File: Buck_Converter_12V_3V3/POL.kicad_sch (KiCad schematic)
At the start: 1 part

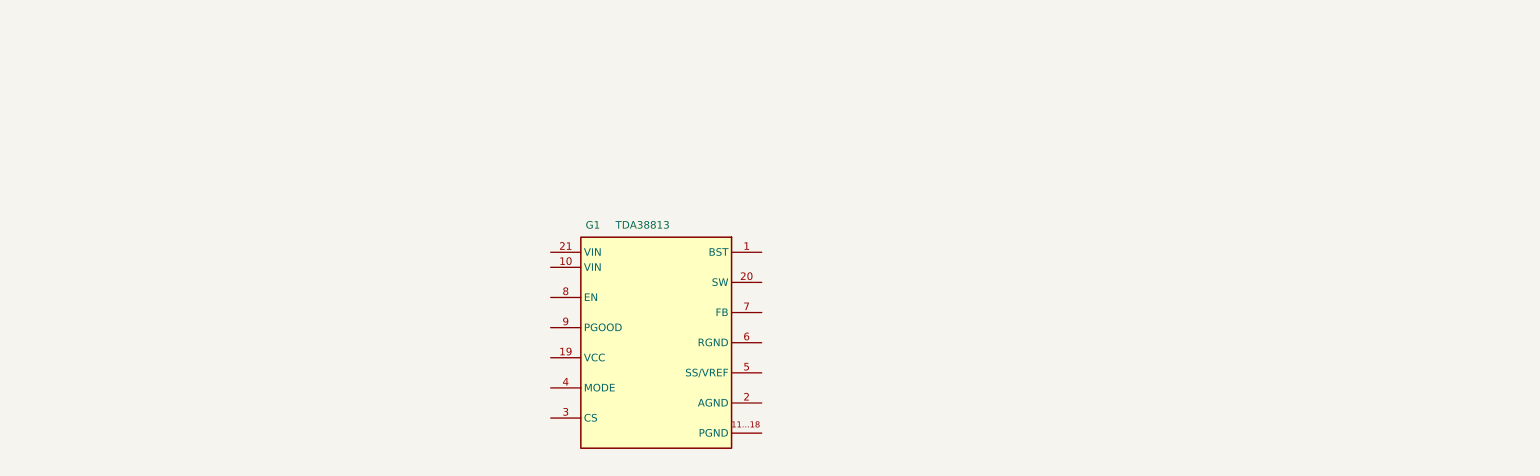
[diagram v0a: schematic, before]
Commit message: :construction: POL IC and input cpacitors added.
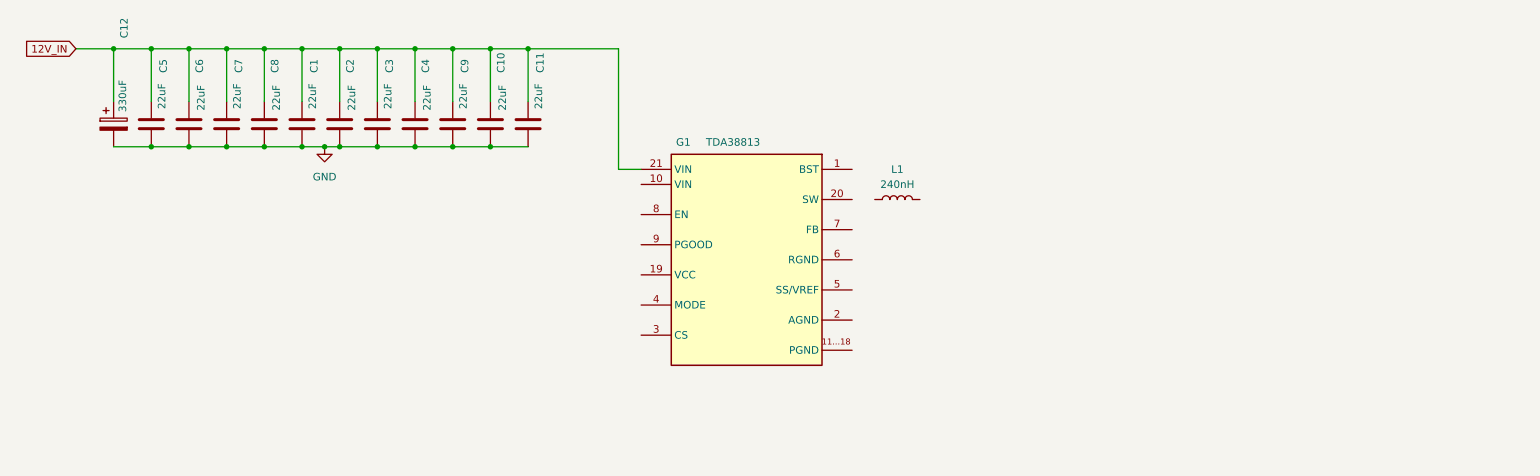
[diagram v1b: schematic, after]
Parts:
- added C1, C10, C11, C2, C3, C4, C5, C6, C7, C8, C9: 22uF, Capacitor_SMD:C_0805_2012Metric_Pad1.18x1.45mm_HandSolder, symbol Device:C
- added C12: 330uF, Capacitor_THT:CP_Radial_D10.0mm_P5.00mm, symbol Device:C_Polarized
- added L1: 240nH, Choke_Coil:Choke_Coil_SMD_3.5_8.4, symbol Device:L
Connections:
- net 12V_IN: now reaches G1.21 (VIN)
- net 12V_IN: now also C1.1, C10.1, C11.1, C12.1, C2.1, C3.1, C4.1, C5.1, C6.1, C7.1, C8.1, C9.1
- new net GND: C1.2, C10.2, C11.2, C12.2, C2.2, C3.2, C4.2, C5.2, C6.2, C7.2, C8.2, C9.2
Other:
- moved on the sheet: G1

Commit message: :construction: Inductor and cap added at power output.
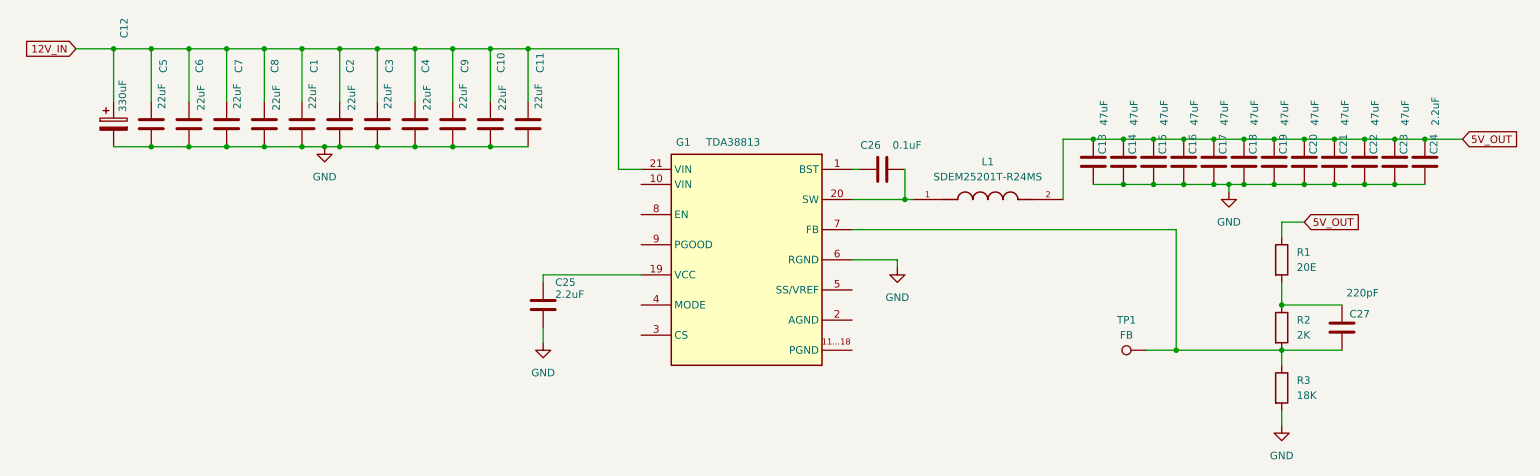
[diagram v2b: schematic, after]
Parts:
- removed L1: 240nH, Choke_Coil:Choke_Coil_SMD_3.5_8.4, symbol Device:L
- added C13, C14, C15, C16, C17, C18, C19, C20, C21, C22, C23: 47uF, Capacitor_SMD:C_0805_2012Metric_Pad1.18x1.45mm_HandSolder, symbol Device:C
- added C24, C25: 2.2uF, Capacitor_SMD:C_0402_1005Metric_Pad0.74x0.62mm_HandSolder, symbol Device:C
- added C26: 0.1uF, Capacitor_SMD:C_0402_1005Metric_Pad0.74x0.62mm_HandSolder, symbol Device:C
- added C27: 220pF, Capacitor_SMD:C_0402_1005Metric_Pad0.74x0.62mm_HandSolder, symbol Device:C
- added L1: SDEM25201T-R24MS, SDEM25201T-R24MS:IND_SDEM25201T-R24MS, symbol Inductor:SDEM25201T-R24MS
- added R1: 20E, Resistor_SMD:R_0402_1005Metric_Pad0.72x0.64mm_HandSolder, symbol Device:R
- added R2: 2K, Resistor_SMD:R_0402_1005Metric_Pad0.72x0.64mm_HandSolder, symbol Device:R
- added R3: 18K, Resistor_SMD:R_0402_1005Metric_Pad0.72x0.64mm_HandSolder, symbol Device:R
- added TP1: FB, symbol Connector:TestPoint
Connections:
- net GND: now also G1.6 (RGND), C13.2, C14.2, C15.2, C16.2, C17.2, C18.2, C19.2, C20.2, C21.2, C22.2, C23.2, C24.2, C25.2, R3.2
- net at G1.1 (BST): now also C26.1
- net at G1.19 (VCC): now also C25.1
- net at G1.20 (SW): now also C26.2, L1.1
- net at G1.7 (FB): now also C27.2, R2.2, R3.1, TP1.1
- new net: C27.1, R1.2, R2.1
- new net 5V_OUT: C13.1, C14.1, C15.1, C16.1, C17.1, C18.1, C19.1, C20.1, C21.1, C22.1, C23.1, C24.1, L1.2, R1.1

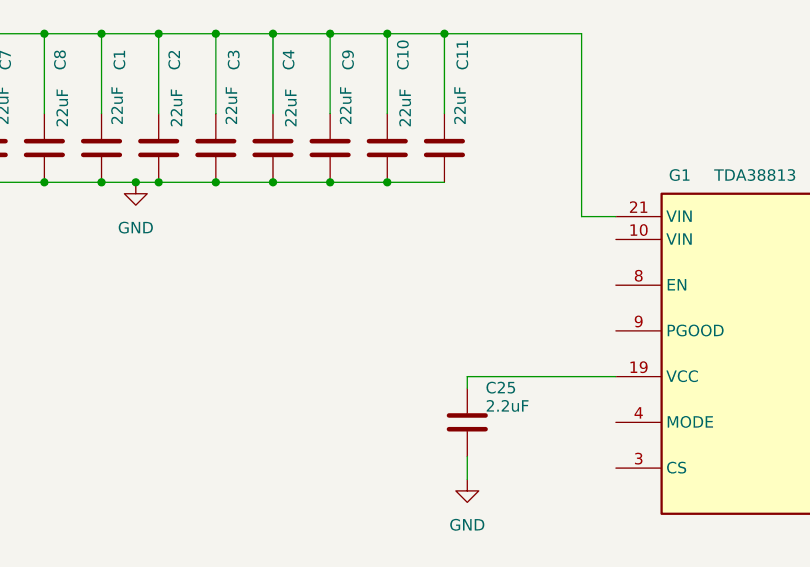
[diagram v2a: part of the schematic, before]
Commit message: Layout Complete
Vis Stiching pending.
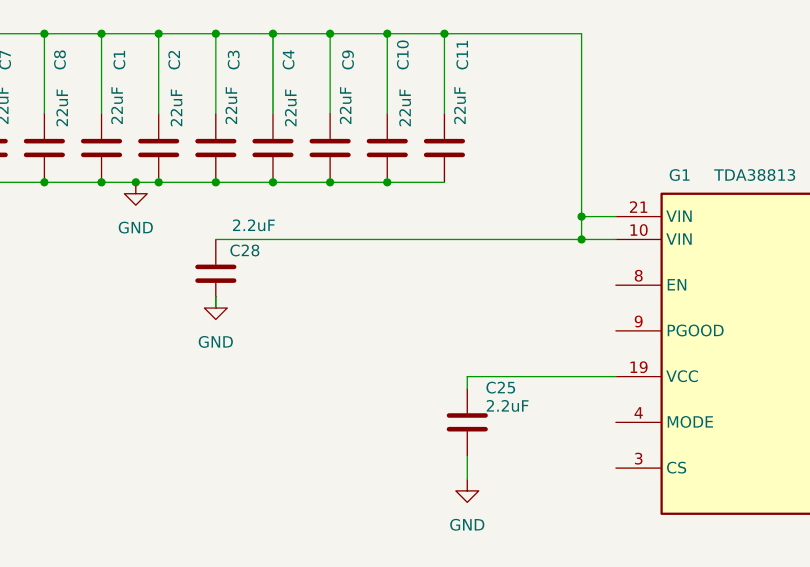
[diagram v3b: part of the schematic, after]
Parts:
- added C28: 2.2uF, Capacitor_SMD:C_0402_1005Metric_Pad0.74x0.62mm_HandSolder, symbol Device:C
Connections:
- net 12V_IN: now also G1.10 (VIN), C28.1
- net GND: now also C28.2
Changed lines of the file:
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@@
 	)
 	(junction
+		(at 128.27 74.93)
+		(diameter 0)
+		(color 0 0 0 0)
+	)
+	(junction
 		(at 113.03 52.07)
 		(diameter 0)
@@
 	)
 	(junction
+		(at 128.27 72.39)
+		(diameter 0)
+		(color 0 0 0 0)
+	)
+	(junction
 		(at 43.18 52.07)
 		(diameter 0)
@@
 	(wire
 		(pts
+			(xy 132.08 74.93) (xy 128.27 74.93)
+		)
+		(stroke
+			(width 0)
+			(type default)
+		)
+	)
+	(wire
+		(pts
 			(xy 55.88 68.58) (xy 62.23 68.58)
 		)
@@
 	(wire
 		(pts
+			(xy 87.63 74.93) (xy 128.27 74.93)
+		)
+		(stroke
+			(width 0)
+			(type default)
+		)
+	)
+	(wire
+		(pts
 			(xy 222.25 102.87) (xy 240.03 102.87)
 		)
@@
 	(wire
 		(pts
+			(xy 87.63 82.55) (xy 87.63 81.28)
+		)
+		(stroke
+			(width 0)
+			(type default)
+		)
+	)
+	(wire
+		(pts
 			(xy 167.64 77.47) (xy 176.53 77.47)
 		)
@@
 	(wire
 		(pts
+			(xy 128.27 72.39) (xy 128.27 74.93)
+		)
+		(stroke
+			(width 0)
+			(type default)
+		)
+	)
+	(wire
+		(pts
 			(xy 43.18 68.58) (xy 49.53 68.58)
 		)
@@
 					(unit 1)
 				)
+			)
+		)
+	)
+	(symbol
+		(lib_id "Device:C")
+		(at 87.63 78.74 0)
+		(unit 1)
+		(exclude_from_sim no)
+		(in_bom yes)
+		(on_board yes)
+		(dnp no)
+		(property "Reference" "C28"
+			(at 89.154 76.2 0)
+			(effects
+				(font
+					(size 1.27 1.27)
+				)
+				(justify left)
+			)
+		)
+		(property "Value" "2.2uF"
+			(at 89.408 73.406 0)
+			(effects
+				(font
+					(size 1.27 1.27)
+				)
+				(justify left)
+			)
+		)
+		(property "Footprint" "Capacitor_SMD:C_0402_1005Metric_Pad0.74x0.62mm_HandSolder"
+			(at 88.5952 82.55 0)
+			(effects
+				(font
+					(size 1.27 1.27)
+				)
+				(hide yes)
+			)
+		)
+		(property "Datasheet" "https://www.digikey.in/en/products/detail/tdk-corporation/C2012X5R0J476M125AC/2443465?s=N4IgTCBcDaIMJgAwEYwA0CsAlRApALAOwBsAsiALoC%2BQA"
+			(at 87.63 78.74 0)
+			(effects
+				(font
+					(size 1.27 1.27)
+				)
+				(hide yes)
+			)
+		)
+		(property "Description" "Unpolarized capacitor"
+			(at 87.63 78.74 0)
+			(effects
+				(font
+					(size 1.27 1.27)
+				)
+				(hide yes)
+			)
+		)
+		(property "Part#" "90-12703-1-ND "
+			(at 87.63 78.74 0)
+			(effects
+				(font
+					(size 1.27 1.27)
+				)
+				(hide yes)
+			)
+		)
+		(pin "2"
+		)
+		(pin "1"
+		)
+		(instances
+			(project "Buck_Converter_12V_3V3"
+				(path "/32fed717-3fa9-48ea-a1a1-4ba9bec3b454/baedb665-4e5c-4013-b239-c7af51cb2ae8"
+					(reference "C28")
+					(unit 1)
+				)
+			)
+		)
+	)
+	(symbol
+		(lib_id "power:GND")
+		(at 87.63 81.28 0)
+		(unit 1)
+		(exclude_from_sim no)
+		(in_bom yes)
+		(on_board yes)
+		(dnp no)
+		(fields_autoplaced yes)
+		(property "Reference" "#PWR06"
+			(at 87.63 87.63 0)
+			(effects
+				(font
+					(size 1.27 1.27)
+				)
+				(hide yes)
+			)
+		)
+		(property "Value" "GND"
+			(at 87.63 86.36 0)
+			(effects
+				(font
+					(size 1.27 1.27)
+				)
+			)
+		)
+		(property "Footprint" ""
+			(at 87.63 81.28 0)
+			(effects
+				(font
+					(size 1.27 1.27)
+				)
+				(hide yes)
+			)
+		)
+		(property "Datasheet" ""
+			(at 87.63 81.28 0)
+			(effects
+				(font
+					(size 1.27 1.27)
+				)
+				(hide yes)
+			)
+		)
+		(property "Description" "Power symbol creates a global label with name \"GND\" , ground"
+			(at 87.63 81.28 0)
+			(effects
+				(font
+					(size 1.27 1.27)
+				)
+				(hide yes)
+			)
+		)
+		(pin "1"
+		)
+		(instances
+			(project "Buck_Converter_12V_3V3"
+				(path "/32fed717-3fa9-48ea-a1a1-4ba9bec3b454/baedb665-4e5c-4013-b239-c7af51cb2ae8"
+					(reference "#PWR06")
+					(unit 1)
+				)
